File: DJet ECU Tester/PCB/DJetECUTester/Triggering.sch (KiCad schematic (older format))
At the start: 12 parts, among them Q5 MMBT2222ALT1G, Q6 MMBT2222ALT1G, Q7 MMBT2222ALT1G, Q8 MMBT2222ALT1G

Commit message: Added injector waveform test points.
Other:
- note removed: "Trigger should go low for 110 degrees of rotation"
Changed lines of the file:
@@
 Text Notes 6000 4450 0    50   ~ 0
 Group IV - E14-PG cyl 7/2 rising edge 180 ATDC
-Text Notes 3000 6100 0    50   ~ 0
-Trigger should go low for 110 degrees of rotation
 $EndSCHEMATC

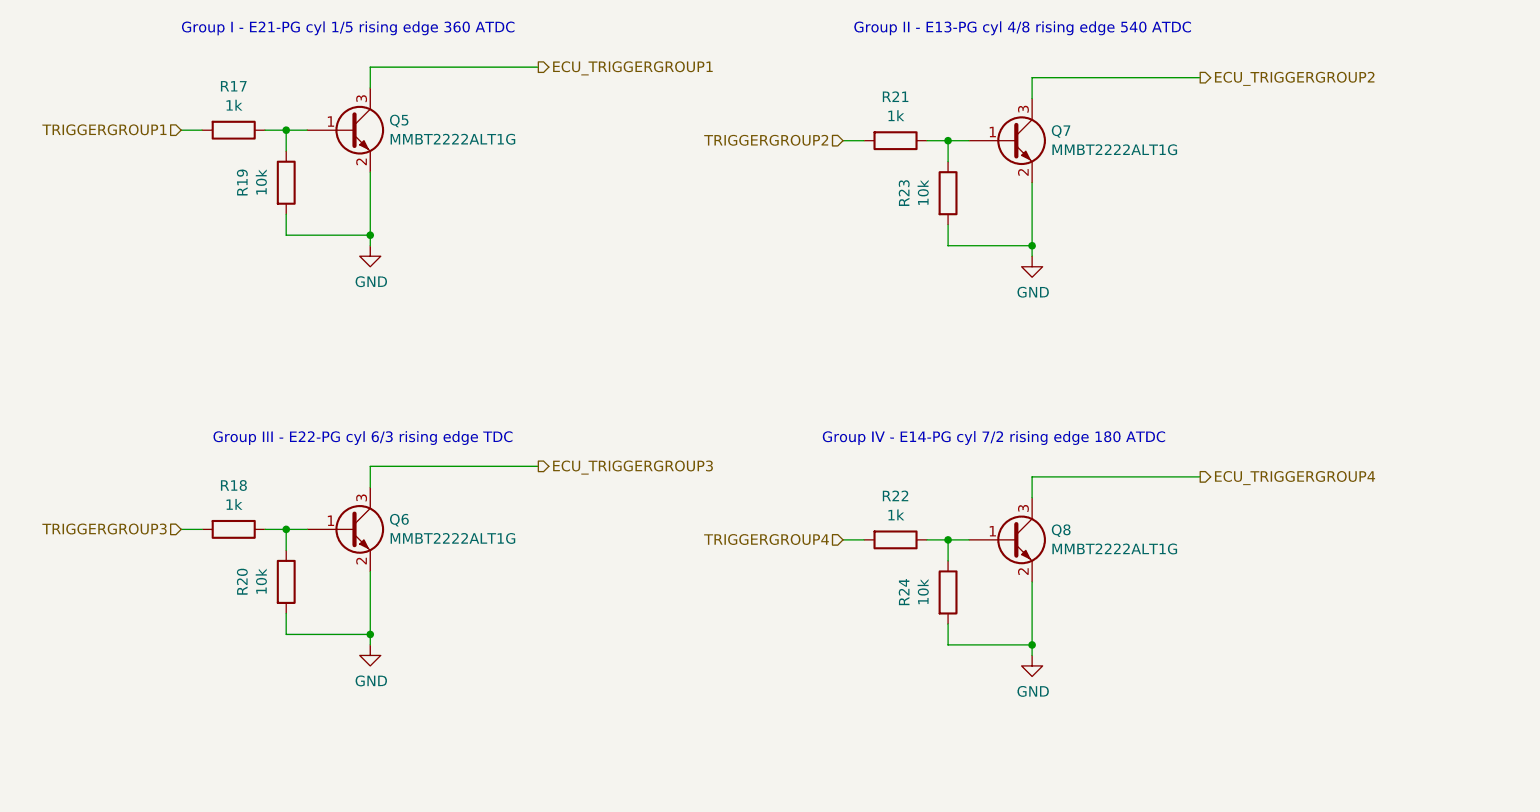
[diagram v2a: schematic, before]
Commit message: Working on PCB layout. Changed CSV circuit from optocoupler to transistors. Added decoupling caps for digital pots.
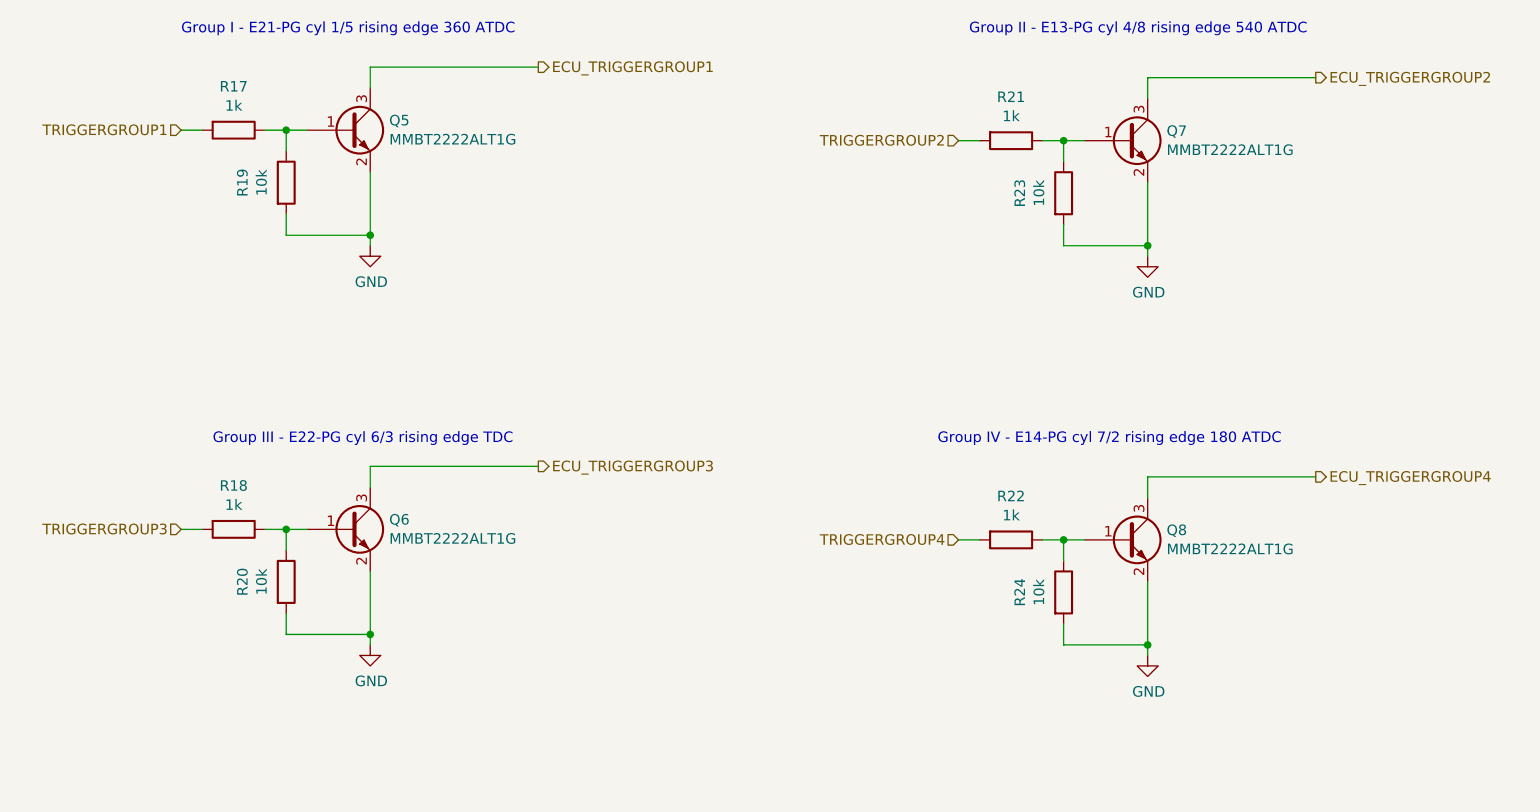
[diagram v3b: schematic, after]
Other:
- moved on the sheet: Q7, Q8, R21, R22, R23, R24
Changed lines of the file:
@@
 Sheet 5 7
 Title "D-Jetronic ECU Tester"
-Date "2021-03-08"
+Date "2021-03-09"
 Rev "1.0"
 Comp "(C) Britishideas 2021"
@@
 L Device:R R21
 U 1 1 60472DFB
-P 6350 3000
-F 0 "R21" V 6143 3000 50  0000 C CNN
-F 1 "1k" V 6234 3000 50  0000 C CNN
-F 2 "Resistor_SMD:R_0805_2012Metric" V 6280 3000 50  0001 C CNN
-F 3 "~" H 6350 3000 50  0001 C CNN
-	1    6350 3000
+P 6900 3000
+F 0 "R21" V 6693 3000 50  0000 C CNN
+F 1 "1k" V 6784 3000 50  0000 C CNN
+F 2 "Resistor_SMD:R_0805_2012Metric" V 6830 3000 50  0001 C CNN
+F 3 "~" H 6900 3000 50  0001 C CNN
+	1    6900 3000
 	0    1    1    0
 $EndComp
@@
 L power:GND #PWR?
 U 1 1 60472E07
-P 7000 3550
+P 7550 3550
 AR Path="/60472E07" Ref="#PWR?"  Part="1"
 AR Path="/604BF505/60472E07" Ref="#PWR?"  Part="1"
 AR Path="/6046850B/60472E07" Ref="#PWR041"  Part="1"
-F 0 "#PWR041" H 7000 3300 50  0001 C CNN
-F 1 "GND" H 7005 3377 50  0000 C CNN
-F 2 "" H 7000 3550 50  0001 C CNN
-F 3 "" H 7000 3550 50  0001 C CNN
-	1    7000 3550
-	1    0    0    -1
-$EndComp
-Wire Wire Line
-	6100 3000 6200 3000
+F 0 "#PWR041" H 7550 3300 50  0001 C CNN
+F 1 "GND" H 7555 3377 50  0000 C CNN
+F 2 "" H 7550 3550 50  0001 C CNN
+F 3 "" H 7550 3550 50  0001 C CNN
+	1    7550 3550
+	1    0    0    -1
+$EndComp
+Wire Wire Line
+	6650 3000 6750 3000
 $Comp
 L Transistor_BJT:MMBT3904 Q7
 U 1 1 60472E0F
-P 6900 3000
-F 0 "Q7" H 7090 3046 50  0000 L CNN
-F 1 "MMBT2222ALT1G" H 7090 2955 50  0000 L CNN
-F 2 "Package_TO_SOT_SMD:SOT-23" H 7100 2925 50  0001 L CIN
-F 3 "https://www.fairchildsemi.com/datasheets/2N/2N3904.pdf" H 6900 3000 50  0001 L CNN
-F 4 "MMBT2222ALT1G" H 6900 3000 50  0001 C CNN "manf#"
-	1    6900 3000
+P 7450 3000
+F 0 "Q7" H 7640 3046 50  0000 L CNN
+F 1 "MMBT2222ALT1G" H 7640 2955 50  0000 L CNN
+F 2 "Package_TO_SOT_SMD:SOT-23" H 7650 2925 50  0001 L CIN
+F 3 "https://www.fairchildsemi.com/datasheets/2N/2N3904.pdf" H 7450 3000 50  0001 L CNN
+F 4 "MMBT2222ALT1G" H 7450 3000 50  0001 C CNN "manf#"
+	1    7450 3000
 	1    0    0    -1
 $EndComp
@@
 L Device:R R23
 U 1 1 60472E15
-P 6600 3250
-F 0 "R23" V 6393 3250 50  0000 C CNN
-F 1 "10k" V 6484 3250 50  0000 C CNN
-F 2 "Resistor_SMD:R_0805_2012Metric" V 6530 3250 50  0001 C CNN
-F 3 "~" H 6600 3250 50  0001 C CNN
-	1    6600 3250
-	1    0    0    -1
-$EndComp
-Wire Wire Line
-	7000 2700 7000 2800
-Wire Wire Line
-	7000 3200 7000 3500
-Wire Wire Line
-	6500 3000 6600 3000
-Wire Wire Line
-	6600 3000 6600 3100
-Connection ~ 6600 3000
-Wire Wire Line
-	6600 3000 6700 3000
-Wire Wire Line
-	6600 3400 6600 3500
-Wire Wire Line
-	6600 3500 7000 3500
-Connection ~ 7000 3500
-Wire Wire Line
-	7000 3500 7000 3550
-Wire Wire Line
-	7000 2700 7800 2700
+P 7150 3250
+F 0 "R23" V 6943 3250 50  0000 C CNN
+F 1 "10k" V 7034 3250 50  0000 C CNN
+F 2 "Resistor_SMD:R_0805_2012Metric" V 7080 3250 50  0001 C CNN
+F 3 "~" H 7150 3250 50  0001 C CNN
+	1    7150 3250
+	1    0    0    -1
+$EndComp
+Wire Wire Line
+	7550 2700 7550 2800
+Wire Wire Line
+	7550 3200 7550 3500
+Wire Wire Line
+	7050 3000 7150 3000
+Wire Wire Line
+	7150 3000 7150 3100
+Connection ~ 7150 3000
+Wire Wire Line
+	7150 3000 7250 3000
+Wire Wire Line
+	7150 3400 7150 3500
+Wire Wire Line
+	7150 3500 7550 3500
+Connection ~ 7550 3500
+Wire Wire Line
+	7550 3500 7550 3550
+Wire Wire Line
+	7550 2700 8350 2700
 $Comp
 L Device:R R22
 U 1 1 60472E2F
-P 6350 4900
-F 0 "R22" V 6143 4900 50  0000 C CNN
-F 1 "1k" V 6234 4900 50  0000 C CNN
-F 2 "Resistor_SMD:R_0805_2012Metric" V 6280 4900 50  0001 C CNN
-F 3 "~" H 6350 4900 50  0001 C CNN
-	1    6350 4900
+P 6900 4900
+F 0 "R22" V 6693 4900 50  0000 C CNN
+F 1 "1k" V 6784 4900 50  0000 C CNN
+F 2 "Resistor_SMD:R_0805_2012Metric" V 6830 4900 50  0001 C CNN
+F 3 "~" H 6900 4900 50  0001 C CNN
+	1    6900 4900
 	0    1    1    0
 $EndComp
@@
 L power:GND #PWR?
 U 1 1 60472E3B
-P 7000 5450
+P 7550 5450
 AR Path="/60472E3B" Ref="#PWR?"  Part="1"
 AR Path="/604BF505/60472E3B" Ref="#PWR?"  Part="1"
 AR Path="/6046850B/60472E3B" Ref="#PWR042"  Part="1"
-F 0 "#PWR042" H 7000 5200 50  0001 C CNN
-F 1 "GND" H 7005 5277 50  0000 C CNN
-F 2 "" H 7000 5450 50  0001 C CNN
-F 3 "" H 7000 5450 50  0001 C CNN
-	1    7000 5450
-	1    0    0    -1
-$EndComp
-Wire Wire Line
-	6100 4900 6200 4900
+F 0 "#PWR042" H 7550 5200 50  0001 C CNN
+F 1 "GND" H 7555 5277 50  0000 C CNN
+F 2 "" H 7550 5450 50  0001 C CNN
+F 3 "" H 7550 5450 50  0001 C CNN
+	1    7550 5450
+	1    0    0    -1
+$EndComp
+Wire Wire Line
+	6650 4900 6750 4900
 $Comp
 L Transistor_BJT:MMBT3904 Q8
 U 1 1 60472E43
-P 6900 4900
-F 0 "Q8" H 7090 4946 50  0000 L CNN
-F 1 "MMBT2222ALT1G" H 7090 4855 50  0000 L CNN
-F 2 "Package_TO_SOT_SMD:SOT-23" H 7100 4825 50  0001 L CIN
-F 3 "https://www.fairchildsemi.com/datasheets/2N/2N3904.pdf" H 6900 4900 50  0001 L CNN
-F 4 "MMBT2222ALT1G" H 6900 4900 50  0001 C CNN "manf#"
-	1    6900 4900
+P 7450 4900
+F 0 "Q8" H 7640 4946 50  0000 L CNN
+F 1 "MMBT2222ALT1G" H 7640 4855 50  0000 L CNN
+F 2 "Package_TO_SOT_SMD:SOT-23" H 7650 4825 50  0001 L CIN
+F 3 "https://www.fairchildsemi.com/datasheets/2N/2N3904.pdf" H 7450 4900 50  0001 L CNN
+F 4 "MMBT2222ALT1G" H 7450 4900 50  0001 C CNN "manf#"
+	1    7450 4900
 	1    0    0    -1
 $EndComp
@@
 L Device:R R24
 U 1 1 60472E49
-P 6600 5150
-F 0 "R24" V 6393 5150 50  0000 C CNN
-F 1 "10k" V 6484 5150 50  0000 C CNN
-F 2 "Resistor_SMD:R_0805_2012Metric" V 6530 5150 50  0001 C CNN
-F 3 "~" H 6600 5150 50  0001 C CNN
-	1    6600 5150
-	1    0    0    -1
-$EndComp
-Wire Wire Line
-	7000 4600 7000 4700
-Wire Wire Line
-	7000 5100 7000 5400
-Wire Wire Line
-	6500 4900 6600 4900
-Wire Wire Line
-	6600 4900 6600 5000
-Connection ~ 6600 4900
-Wire Wire Line
-	6600 4900 6700 4900
-Wire Wire Line
-	6600 5300 6600 5400
-Wire Wire Line
-	6600 5400 7000 5400
-Connection ~ 7000 5400
-Wire Wire Line
-	7000 5400 7000 5450
-Wire Wire Line
-	7000 4600 7800 4600
+P 7150 5150
+F 0 "R24" V 6943 5150 50  0000 C CNN
+F 1 "10k" V 7034 5150 50  0000 C CNN
+F 2 "Resistor_SMD:R_0805_2012Metric" V 7080 5150 50  0001 C CNN
+F 3 "~" H 7150 5150 50  0001 C CNN
+	1    7150 5150
+	1    0    0    -1
+$EndComp
+Wire Wire Line
+	7550 4600 7550 4700
+Wire Wire Line
+	7550 5100 7550 5400
+Wire Wire Line
+	7050 4900 7150 4900
+Wire Wire Line
+	7150 4900 7150 5000
+Connection ~ 7150 4900
+Wire Wire Line
+	7150 4900 7250 4900
+Wire Wire Line
+	7150 5300 7150 5400
+Wire Wire Line
+	7150 5400 7550 5400
+Connection ~ 7550 5400
+Wire Wire Line
+	7550 5400 7550 5450
+Wire Wire Line
+	7550 4600 8350 4600
 Text HLabel 4650 2650 2    50   Output ~ 0
 ECU_TRIGGERGROUP1
-Text HLabel 7800 2700 2    50   Output ~ 0
+Text HLabel 8350 2700 2    50   Output ~ 0
 ECU_TRIGGERGROUP2
 Text HLabel 4650 4550 2    50   Output ~ 0
 ECU_TRIGGERGROUP3
-Text HLabel 7800 4600 2    50   Output ~ 0
+Text HLabel 8350 4600 2    50   Output ~ 0
 ECU_TRIGGERGROUP4
 Text HLabel 2950 2950 0    50   Input ~ 0
@@
 Text HLabel 2950 4850 0    50   Input ~ 0
 TRIGGERGROUP3
-Text HLabel 6100 3000 0    50   Input ~ 0
+Text HLabel 6650 3000 0    50   Input ~ 0
 TRIGGERGROUP2
-Text HLabel 6100 4900 0    50   Input ~ 0
+Text HLabel 6650 4900 0    50   Input ~ 0
 TRIGGERGROUP4
 Text Notes 2950 2500 0    50   ~ 0
 Group I - E21-PG cyl 1/5 rising edge 360 ATDC
-Text Notes 6150 2500 0    50   ~ 0
+Text Notes 6700 2500 0    50   ~ 0
 Group II - E13-PG cyl 4/8 rising edge 540 ATDC\n
 Text Notes 3100 4450 0    50   ~ 0
 Group III - E22-PG cyl 6/3 rising edge TDC
-Text Notes 6000 4450 0    50   ~ 0
+Text Notes 6550 4450 0    50   ~ 0
 Group IV - E14-PG cyl 7/2 rising edge 180 ATDC
 $EndSCHEMATC
